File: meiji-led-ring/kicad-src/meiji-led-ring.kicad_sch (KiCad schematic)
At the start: 66 parts, among them J1 USB_C_Receptacle_USB2.0, U1 ATSAML10D14-MFT, U2 AP5726, U3 AP5726, U4 MCP1700-3302E_SOT23

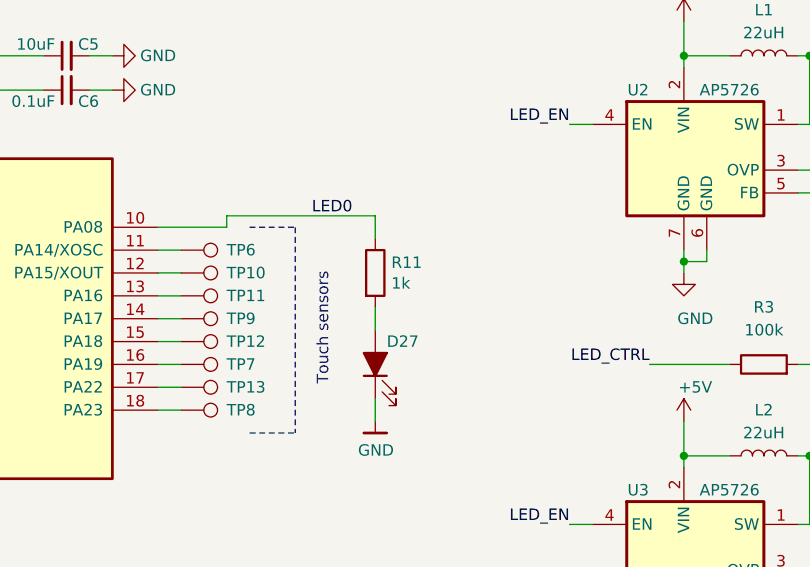
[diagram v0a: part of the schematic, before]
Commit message: meji-led-ring: Add BOM values to project
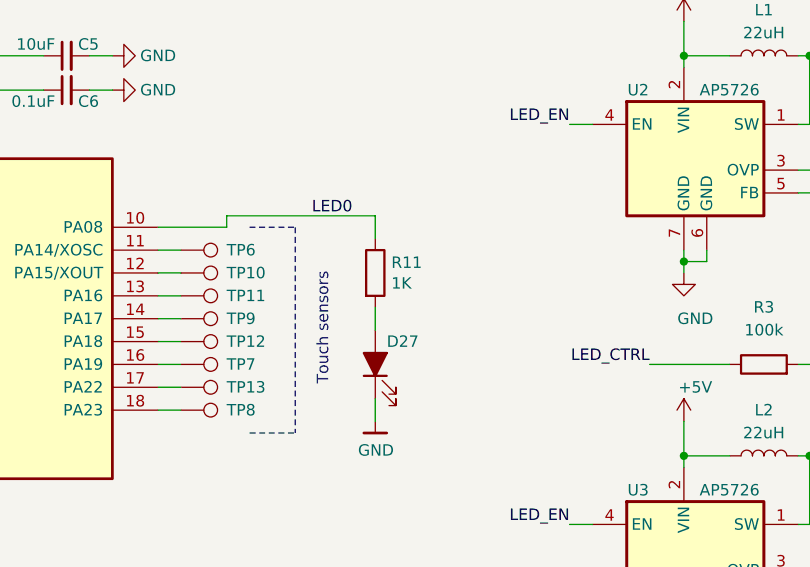
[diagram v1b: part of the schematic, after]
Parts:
- C1, C2: Mfg (none) -> Taiyo Yuden; PN (none) -> TMK325B7226KM-PR
- C3, C4: Mfg (none) -> Yageo; PN (none) -> CC0402KRX5R8BB105
- C5: Mfg (none) -> Taiyo Yuden; PN (none) -> LDK105CBJ106MVLF
- C6, C7: Mfg (none) -> Yageo; PN (none) -> CC0402JRX7R7BB104
- D1, D10, D11, D12, D13, D14, D15, D16, D17, D18, D19, D2, D20, D21, D22, D23, D24, D3, D4, D5, D6, D7, D8, D9: Mfg (none) -> Lextar; PN (none) -> PC30H08-V4
- D27: Mfg (none) -> TOGIALED; PN (none) -> TJ-S1005SW4TGLC7K-A5
- J1: Mfg (none) -> Jing Extension of the Electronic Co.; PN (none) -> C167321
- R1, R2, R5, R6: Mfg (none) -> Yageo; PN (none) -> AC0402FR-075K1L
- R10, R7, R8, R9: Mfg (none) -> UNI-ROYAL(Uniroyal Elec); PN (none) -> 0603WAF100JT5E
- R11: value 1k -> 1K; Mfg (none) -> Yageo; PN (none) -> AC0402FR-071KL
- R14: Mfg (none) -> Yageo; PN (none) -> AC0402FR-071KL
- R3, R4: Mfg (none) -> Yageo; PN (none) -> AC0402FR-07100KL
- U1: Mfg (none) -> Microchip Technology; PN (none) -> ATSAML10D14A-MUTCT-ND
- U2, U3: Mfg (none) -> Diodes Incorporated; PN (none) -> AP5726FDCG-7
- U4: LCSC C83932 -> (none); Mfg (none) -> Microchip Technology; PN (none) -> MCP1700T-3302E/TT
